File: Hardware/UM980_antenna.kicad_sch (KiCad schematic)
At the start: 18 parts, among them J5 SMA_EdgeMount, Q2 DMG2305UX, U3 MCP6021T, U4 74LVC2G07, U6 74LVC2G07

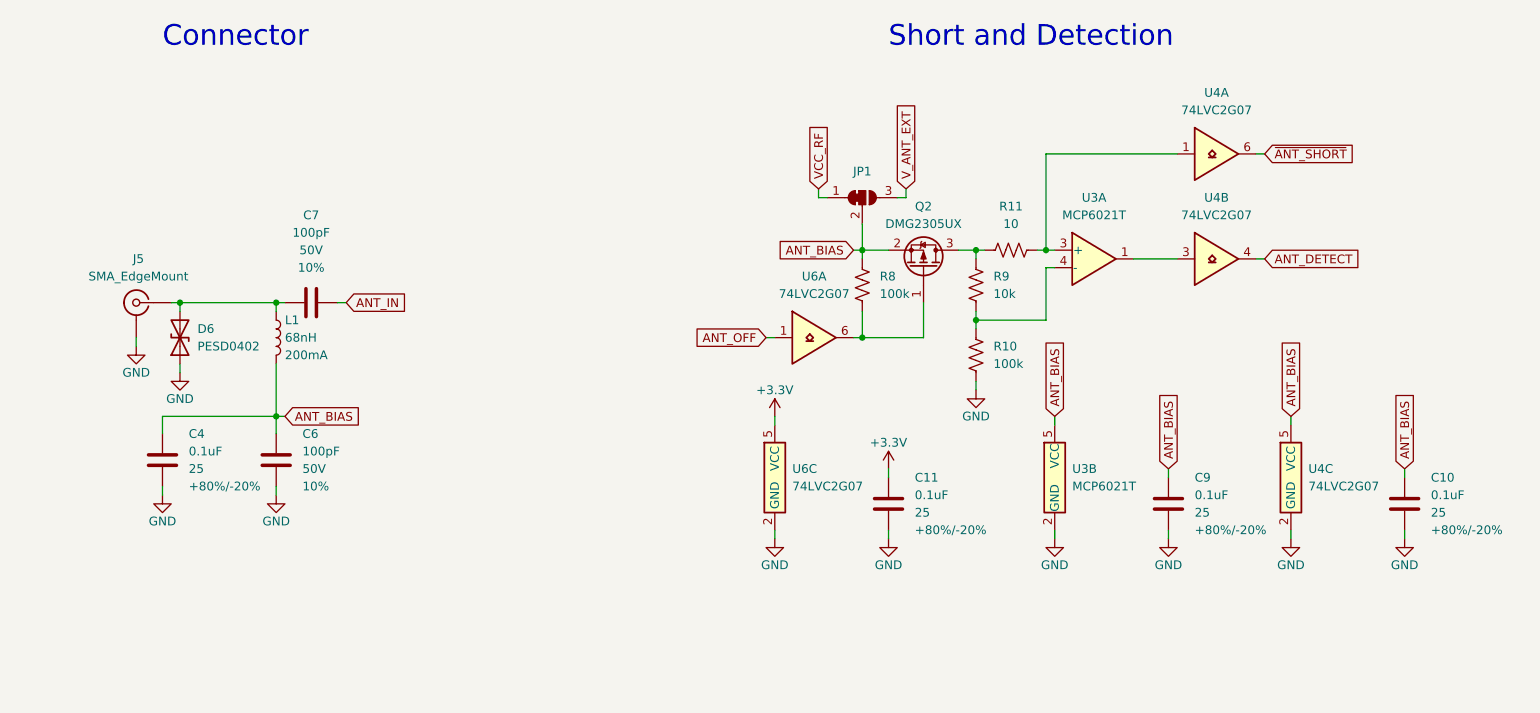
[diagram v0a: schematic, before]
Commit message: Update design with PROD_IDs
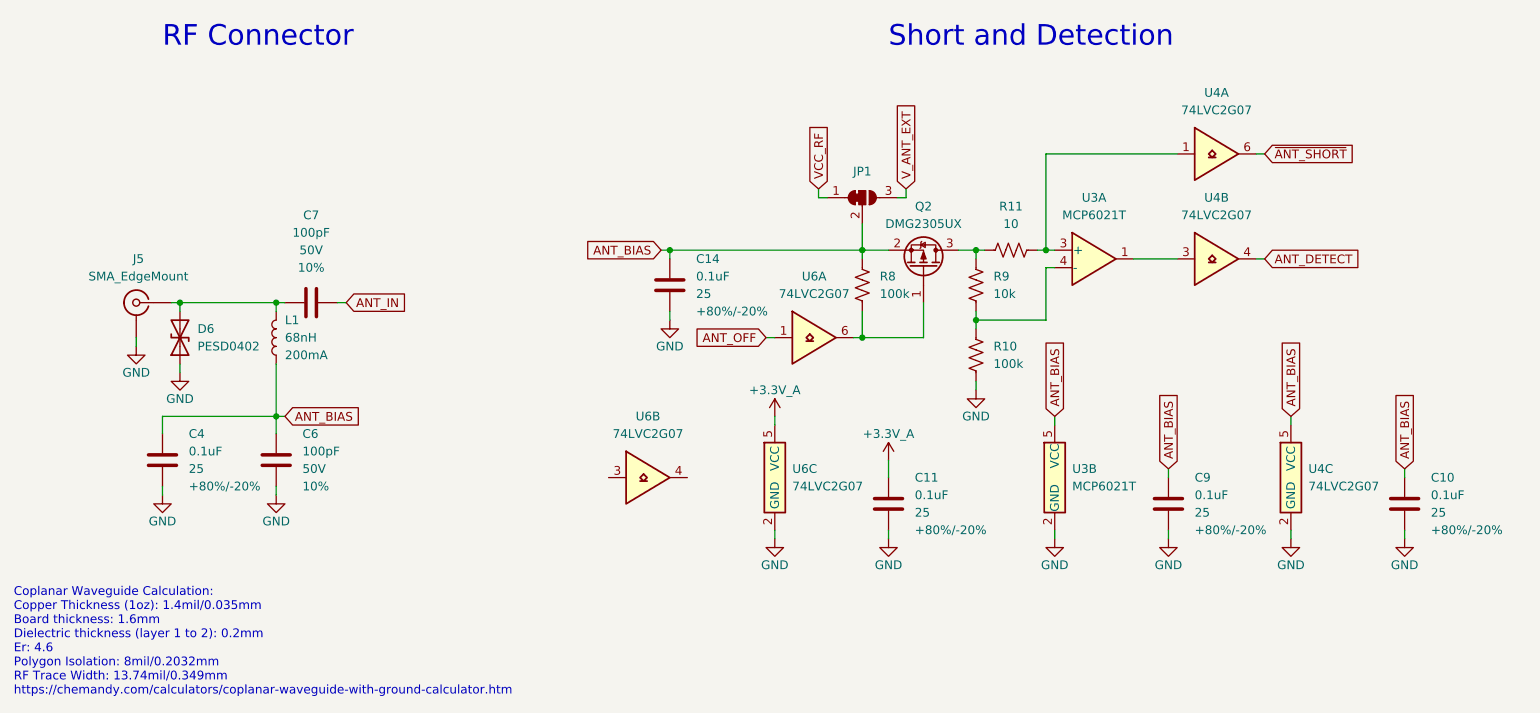
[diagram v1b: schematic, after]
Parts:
- added C14: 0.1uF, SparkFun-Capacitor:C_0603_1608Metric, symbol SparkFun-Capacitor:0.1uF_0603_25V_20%
- added unit 2 of U6
- C10, C11, C4, C9: PROD_ID 810 -> CAP-00810
- C6, C7: PROD_ID 7883 -> CAP-07883
- D6: PROD_ID 15359 -> DIO-15359
- J5: PROD_ID 8289 -> CONN-08289
- L1: PROD_ID 15356 -> NDUC-15356
- Q2: PROD_ID 11308 -> TRANS-11308
- R10, R8: PROD_ID 7828 -> RES-07828
- R11: PROD_ID 8705 -> RES-08705
- R9: PROD_ID 824 -> RES-00824
- U3: PROD_ID 12504 -> IC-12504
- U4, U6: PROD_ID (none) -> IC-19693
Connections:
- net ANT_BIAS: now also L1.1, C14.1; no longer L1.2
- net GND: now also C14.2
- net at C7.1, D6.2 (A2), J5.SIG (In): now also L1.2; no longer L1.1
- net +3.3V renamed +3.3V_A
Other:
- note added: "Coplanar Waveguide Calculation: Copper Thickness (1oz): 1.4mil/0.035mm Board thickness: 1.6mm Dielectric thickness (layer 1 to 2): 0.2mm Er: 4.6 Polygon Isolation: 8mil/0.2032mm RF Trace Width: 13.74mil/0.349mm https://chemandy.com/calculators/coplanar-waveguide-with-ground-calculator.htm"
- note added: "RF Connector"
- note removed: "Connector"
- moved on the sheet: L1

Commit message: Change port 3 to be compatible with BlueSMiRF
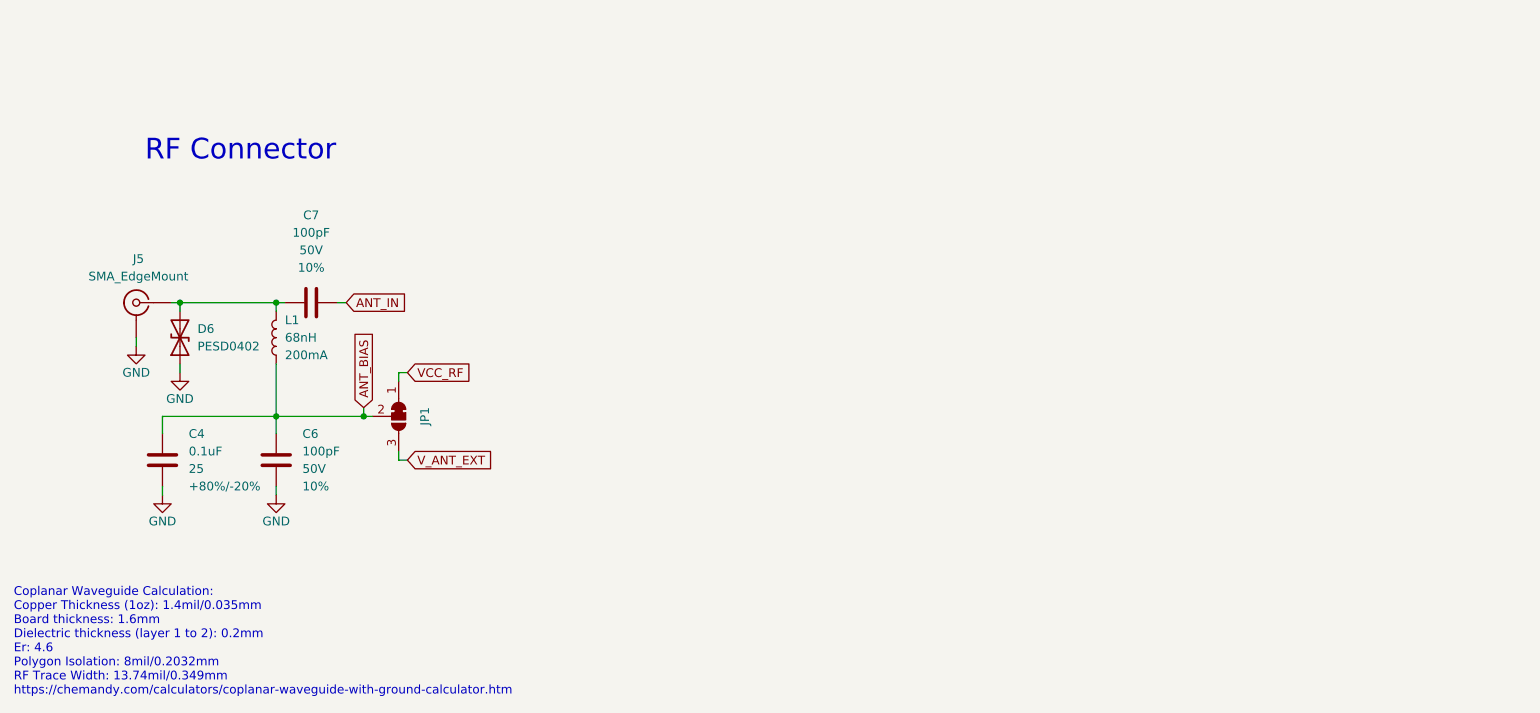
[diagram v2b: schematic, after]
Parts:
- removed C10, C11, C14, C9: 0.1uF, SparkFun-Capacitor:C_0603_1608Metric, symbol SparkFun-Capacitor:0.1uF_0603_25V_20%
- removed Q2: DMG2305UX, SparkFun-Semiconductor-Standard:SOT23-3, symbol SparkFun-DiscreteSemi:PMOS_4.2A_20V
- removed R10, R8: 100k, SparkFun-Resistor:R_0603_1608Metric, symbol SparkFun-Resistor:100k_0603
- removed R11: 10, SparkFun-Resistor:R_1206_3216Metric, symbol SparkFun-Resistor:10_1206
- removed R9: 10k, SparkFun-Resistor:R_0603_1608Metric, symbol SparkFun-Resistor:10k_0603
- removed U3: MCP6021T, SparkFun-Semiconductor-Standard:SOT23-5, symbol SparkFun-IC-Amplifier:OPAMP_MCP6021T
- removed U4, U6: 74LVC2G07, SparkFun-Semiconductor-Standard:SOT23-6, symbol SparkFun-IC-Logic:74LVC2G07
- D6: symbol SparkFun-DiscreteSemi:Diode_TVS_0402 -> SparkFun-DiscreteSemi:D_TVS_0402
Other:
- note removed: "Short and Detection"
- moved on the sheet: JP1

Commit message: Post design review.
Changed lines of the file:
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@@
     (pin "2")
     (instances
-      (project "SparkFun_UM980_panelized"
+      (project "SparkFun_GNSS_UM980"
         (path "/e3dd3ae4-244d-4cba-9cca-5d2abf83f29a/4d8e7a61-3b13-4db6-8f5b-1b3bc0074024"
           (reference "L1") (unit 1)
@@
     (pin "1")
     (instances
-      (project "SparkFun_UM980_panelized"
+      (project "SparkFun_GNSS_UM980"
         (path "/e3dd3ae4-244d-4cba-9cca-5d2abf83f29a"
           (reference "#PWR031") (unit 1)
@@
     (pin "2")
     (instances
-      (project "SparkFun_UM980_panelized"
+      (project "SparkFun_GNSS_UM980"
         (path "/e3dd3ae4-244d-4cba-9cca-5d2abf83f29a/4d8e7a61-3b13-4db6-8f5b-1b3bc0074024"
           (reference "C4") (unit 1)
@@
     (pin "1")
     (instances
-      (project "SparkFun_UM980_panelized"
+      (project "SparkFun_GNSS_UM980"
         (path "/e3dd3ae4-244d-4cba-9cca-5d2abf83f29a"
           (reference "#PWR032") (unit 1)
@@
     (pin "1")
     (instances
-      (project "SparkFun_UM980_panelized"
+      (project "SparkFun_GNSS_UM980"
         (path "/e3dd3ae4-244d-4cba-9cca-5d2abf83f29a"
           (reference "#PWR033") (unit 1)
@@
     (pin "2")
     (instances
-      (project "SparkFun_UM980_panelized"
+      (project "SparkFun_GNSS_UM980"
         (path "/e3dd3ae4-244d-4cba-9cca-5d2abf83f29a/4d8e7a61-3b13-4db6-8f5b-1b3bc0074024"
           (reference "D6") (unit 1)
@@
     (pin "1")
     (instances
-      (project "SparkFun_UM980_panelized"
+      (project "SparkFun_GNSS_UM980"
         (path "/e3dd3ae4-244d-4cba-9cca-5d2abf83f29a"
           (reference "#PWR030") (unit 1)
@@
     (pin "3")
     (instances
-      (project "SparkFun_UM980_panelized"
+      (project "SparkFun_GNSS_UM980"
         (path "/e3dd3ae4-244d-4cba-9cca-5d2abf83f29a/4d8e7a61-3b13-4db6-8f5b-1b3bc0074024"
           (reference "JP1") (unit 1)
@@
     (pin "2")
     (instances
-      (project "SparkFun_UM980_panelized"
+      (project "SparkFun_GNSS_UM980"
         (path "/e3dd3ae4-244d-4cba-9cca-5d2abf83f29a/4d8e7a61-3b13-4db6-8f5b-1b3bc0074024"
           (reference "C7") (unit 1)
@@
     (pin "SIG")
     (instances
-      (project "SparkFun_UM980_panelized"
+      (project "SparkFun_GNSS_UM980"
         (path "/e3dd3ae4-244d-4cba-9cca-5d2abf83f29a/4d8e7a61-3b13-4db6-8f5b-1b3bc0074024"
           (reference "J5") (unit 1)
@@
     (pin "2")
     (instances
-      (project "SparkFun_UM980_panelized"
+      (project "SparkFun_GNSS_UM980"
         (path "/e3dd3ae4-244d-4cba-9cca-5d2abf83f29a/4d8e7a61-3b13-4db6-8f5b-1b3bc0074024"
           (reference "C6") (unit 1)

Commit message: Update to v8. Update models.
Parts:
- C4: Tolerance +80%/-20% -> 20%; Voltage 25 -> 25V
- D6: value PESD0402 -> PESD0402
- J5: value SMA_EdgeMount -> SMA_Edge; footprint SparkFun-Connector:SMA-EDGE -> SparkFun-Connector:SMA_Edge
- JP1: footprint SparkFun-Jumper:SMT-JUMPER_3_1-NC_TRACE_SILK -> SparkFun-Jumper:Jumper_3_NC-1_Trace
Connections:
- net GND: no longer J5.1, J5.3, J5.4
- net at C7.1, D6.2 (A2), L1.2: now also J5.1 (In); no longer J5.SIG (In)
